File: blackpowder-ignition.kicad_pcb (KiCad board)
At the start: 4 copper layers, 63.5 x 63.5 mm, 54 parts, among them J1 CAS_stacking, J10 Conn_01x02, J2 Conn_01x02, J3 Conn_01x02, J4 Conn_01x02, J5 Conn_01x02, J6 Conn_01x02, J7 Conn_01x02, J8 Conn_01x02, J9 Conn_01x02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

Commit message: updates based on review
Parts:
- added C10: 100nF, Capacitor_SMD:C_0603_1608Metric_Pad1.08x0.95mm_HandSolder, F.Cu at (42.7, 63.0)
- added C2: 100nF, Capacitor_SMD:C_0603_1608Metric_Pad1.08x0.95mm_HandSolder, F.Cu at (31.6, 76.1)
- added C3: 4.7uF, Capacitor_SMD:C_0603_1608Metric_Pad1.08x0.95mm_HandSolder, F.Cu at (72.1, 55.1)
- added C4: 100nF, Capacitor_SMD:C_0603_1608Metric_Pad1.08x0.95mm_HandSolder, F.Cu at (70.4, 55.1)
- added C5: 4.7uF, Capacitor_SMD:C_0603_1608Metric_Pad1.08x0.95mm_HandSolder, F.Cu at (55.3, 55.1)
- added C6: 100nF, Capacitor_SMD:C_0603_1608Metric_Pad1.08x0.95mm_HandSolder, F.Cu at (53.6, 55.1)
- added C7: 4.7uF, Capacitor_SMD:C_0603_1608Metric_Pad1.08x0.95mm_HandSolder, F.Cu at (39.1, 55.0)
- added C8: 100nF, Capacitor_SMD:C_0603_1608Metric_Pad1.08x0.95mm_HandSolder, F.Cu at (37.3, 55.0)
- added C9: 4.7uF, Capacitor_SMD:C_0603_1608Metric_Pad1.08x0.95mm_HandSolder, F.Cu at (40.9, 63.0)
- added R25: 10k, Resistor_SMD:R_0603_1608Metric_Pad0.98x0.95mm_HandSolder, F.Cu at (42.7, 82.8)
- added R26: 10k, Resistor_SMD:R_0603_1608Metric_Pad0.98x0.95mm_HandSolder, F.Cu at (39.9, 82.8)
- added R27: 10k, Resistor_SMD:R_0603_1608Metric_Pad0.98x0.95mm_HandSolder, F.Cu at (36.8, 82.8)
- U2, U3, U4, U5: value TC4427AVOA -> MSOP8_MC_MCH; footprint Package_SO:MSOP-8-1EP_3x3mm_P0.65mm_EP2.5x3mm_Mask1.73x2.36mm -> star-common-lib:TC4427AEUA
- moved R20 10.1 mm to (45.6, 57.5), turned to 0 degrees
- moved R19 8.36 mm to (49.1, 57.5)
- moved R23 5.33 mm to (53.8, 73.9)
- moved R12 3.56 mm to (63.8, 51.9)
- moved R18 3.56 mm to (47.5, 52.3)
- moved R6 3.56 mm to (80.5, 51.8)
- moved R14 2.80 mm to (45.6, 55.9)
- moved U5 2.75 mm to (45.5, 62.7), turned to 270 degrees
- moved R16 1.78 mm to (49.3, 52.3)
- moved R4 1.78 mm to (82.3, 51.8)
- moved R10 1.78 mm to (65.5, 51.9)
- moved R17 1.78 mm to (51.1, 52.3)
- moved R21 1.78 mm to (48.5, 73.9)
- moved R22 1.78 mm to (52.1, 73.9)
- moved R24 1.78 mm to (50.3, 73.9)
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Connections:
- net Net-(Q1-Pad2) renamed /IgnitionAB/igniteA_driven
- net Net-(Q1-Pad4) renamed /IgnitionAB/igniteB_driven
- net Net-(Q3-Pad2) renamed /IgnitionCD/igniteA_driven
- net Net-(Q3-Pad4) renamed /IgnitionCD/igniteB_driven
- net Net-(Q5-Pad2) renamed /IgnitionEF/igniteA_driven
- net Net-(Q5-Pad4) renamed /IgnitionEF/igniteB_driven
- net Net-(Q7-Pad2) renamed /IgnitionGH/igniteA_driven
- net Net-(Q7-Pad4) renamed /IgnitionGH/igniteB_driven
- J8 pad 1: +BATT -> GND
- J8 pad 2: GND -> +BATT
- JP1 pad 3: +3V3 -> Net-(JP1-Pad3)
- JP2 pad 3: +3V3 -> Net-(JP2-Pad3)
- JP3 pad 3: +3V3 -> Net-(JP3-Pad3)
- Q2 pad 1: /~contB~ -> +3V3
- Q2 pad 3: +3V3 -> /~contA~
- Q2 pad 4: /~contA~ -> +3V3
- Q2 pad 6: +3V3 -> /~contB~
- Q4 pad 1: /~contD~ -> +3V3
- Q4 pad 3: +3V3 -> /~contC~
- Q4 pad 4: /~contC~ -> +3V3
- Q4 pad 6: +3V3 -> /~contD~
- Q6 pad 1: /~contF~ -> +3V3
- Q6 pad 3: +3V3 -> /~contE~
- Q6 pad 4: /~contE~ -> +3V3
- Q6 pad 6: +3V3 -> /~contF~
- Q8 pad 1: /~contH~ -> +3V3
- Q8 pad 3: +3V3 -> /~contG~
- Q8 pad 4: /~contG~ -> +3V3
- Q8 pad 6: +3V3 -> /~contH~
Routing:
- net GND: track 93.6 -> 134.7 mm, vias 41 -> 38
- net +5V: track 94.6 -> 112.2 mm, vias 4 -> 7
- net +3V3: track 22.2 -> 33.0 mm, vias 10 -> 6
- net /igniteG: track 8.06 -> 17.7 mm, vias 0 -> 2
- net /igniteH: track 17.6 -> 24.8 mm
- net /~contG~: track 26.9 -> 21.2 mm
- net /~contH~: track 21.9 -> 26.1 mm
- net /~contA~: track 58.2 -> 54.5 mm
- net /~contE~: track 33.6 -> 30.4 mm
- net /~contC~: track 38.1 -> 35.0 mm
- net /~contB~: track 56.8 -> 59.3 mm
- net /~contD~: track 39.5 -> 41.7 mm
- net /IgnitionGH/igniteB_driven: track 4.00 -> 6.11 mm
- net Net-(JP2-Pad3): track 0.00 -> 2.03 mm
- net Net-(JP3-Pad3): track 0.00 -> 1.98 mm
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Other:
- net class Default: clearance 0.2032 -> 0.1524
- rule trace_clearance: 0.2032 -> 0.1524

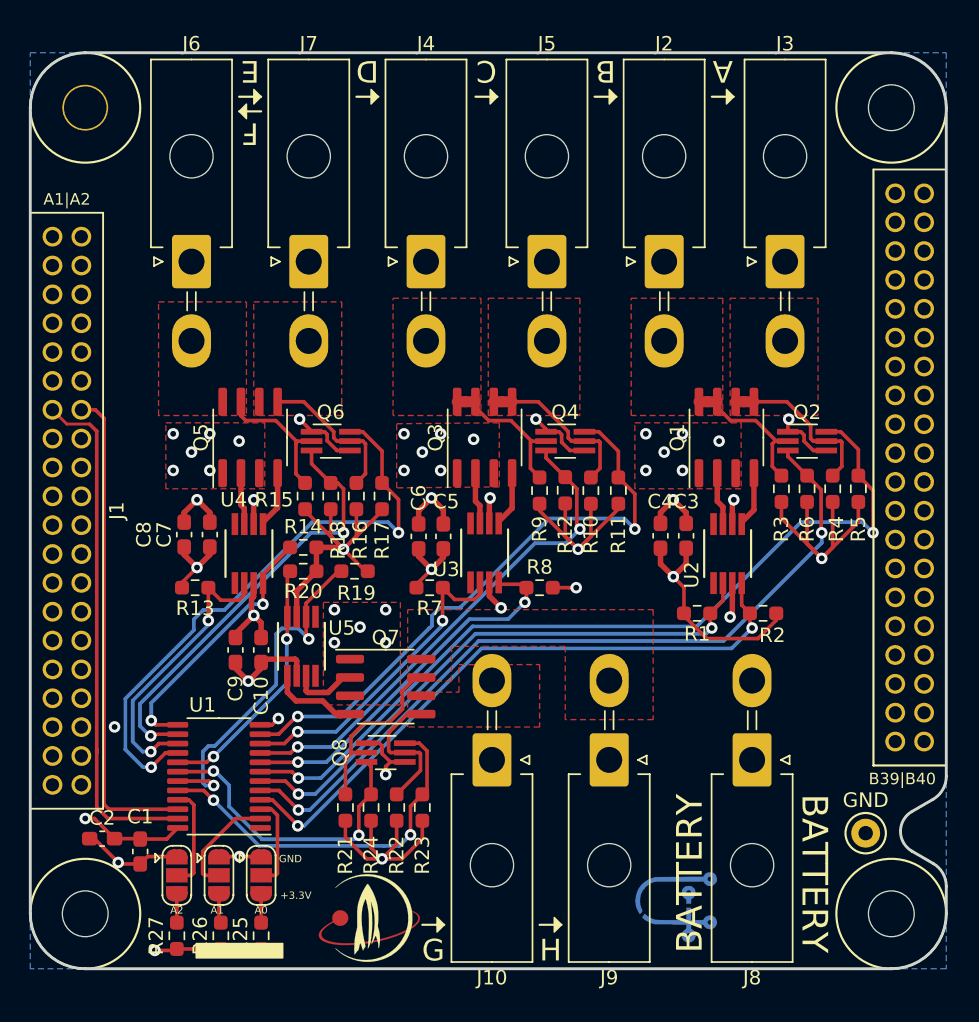
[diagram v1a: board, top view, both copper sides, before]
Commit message: added diodes for esd
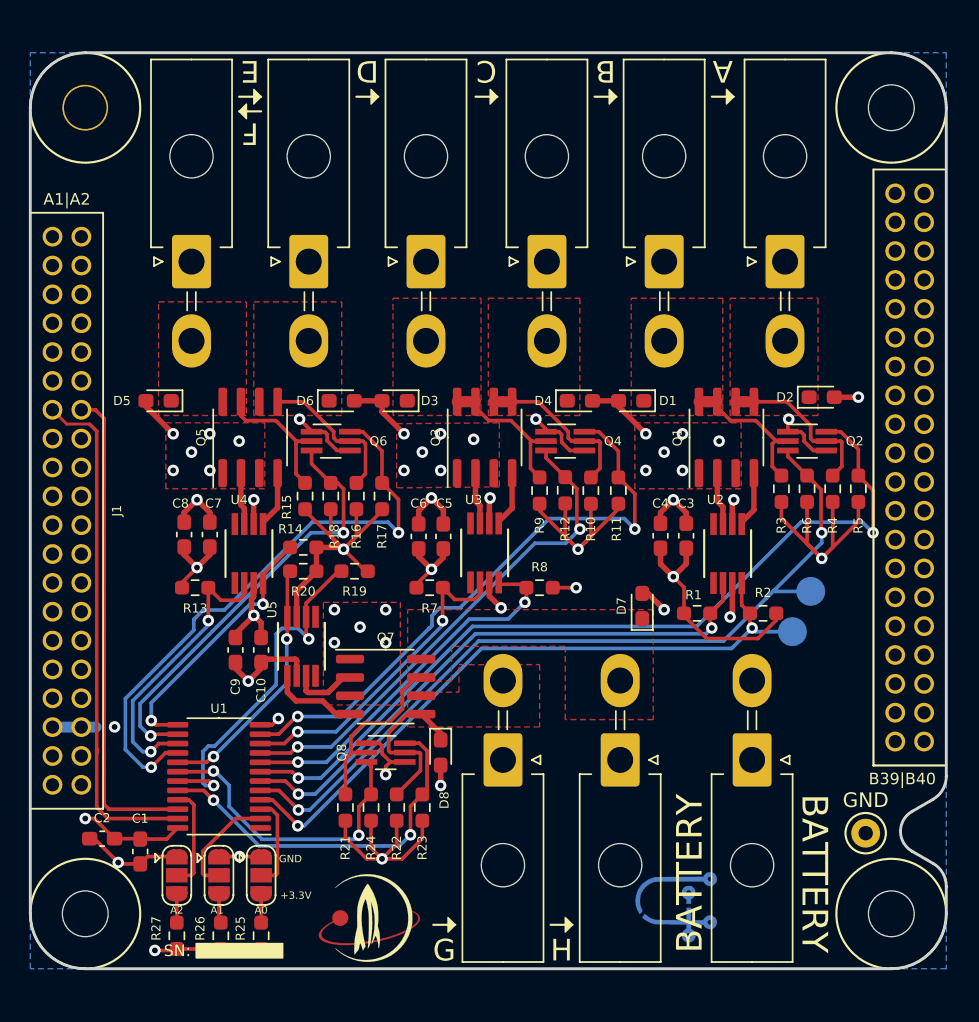
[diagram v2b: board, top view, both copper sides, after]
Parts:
- added D1: D_Zener, Diode_SMD:D_0603_1608Metric_Pad1.05x0.95mm_HandSolder, F.Cu at (68.3, 45.7)
- added D2: D_Zener, Diode_SMD:D_0603_1608Metric_Pad1.05x0.95mm_HandSolder, F.Cu at (81.5, 45.5)
- added D3: D_Zener, Diode_SMD:D_0603_1608Metric_Pad1.05x0.95mm_HandSolder, F.Cu at (51.9, 45.7)
- added D4: D_Zener, Diode_SMD:D_0603_1608Metric_Pad1.05x0.95mm_HandSolder, F.Cu at (64.8, 45.7)
- added D5: D_Zener, Diode_SMD:D_0603_1608Metric_Pad1.05x0.95mm_HandSolder, F.Cu at (35.6, 45.7)
- added D6: D_Zener, Diode_SMD:D_0603_1608Metric_Pad1.05x0.95mm_HandSolder, F.Cu at (48.3, 45.7)
- added D7: D_Zener, Diode_SMD:D_0603_1608Metric_Pad1.05x0.95mm_HandSolder, F.Cu at (69.1, 59.9)
- added D8: D_Zener, Diode_SMD:D_0603_1608Metric_Pad1.05x0.95mm_HandSolder, F.Cu at (55.1, 70.1)
- added REF**: TestPoint_Pad_D2.0mm, TestPoint:TestPoint_Pad_D2.0mm, B.Cu at (80.8, 58.9)
- added REF**: TestPoint_Pad_D2.0mm, TestPoint:TestPoint_Pad_D2.0mm, B.Cu at (79.5, 61.7)
- moved J10 0.76 mm to (59.4, 70.6)
- moved J9 0.76 mm to (67.6, 70.6)
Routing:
- net GND: track 134.7 -> 152.5 mm, vias 38 -> 41
- net +3V3: track 33.0 -> 36.0 mm
- net /igniteA: track 43.8 -> 46.7 mm
- net /~contA~: track 54.5 -> 57.1 mm
- net Net-(D8-Pad1): track 9.85 -> 12.2 mm
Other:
- board text added: "IgniteA"
- board text added: "~contA~"
